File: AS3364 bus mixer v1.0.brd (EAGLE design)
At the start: 44.5 x 32.4 mm, 65 parts, among them IC1 TL072JT, IC2 TL072JT, IC3 TL072JT, IC30 TL072JT, IC4 TL072JT, IC5 79L09F, IC6 78L09F, IC7 CH446Q

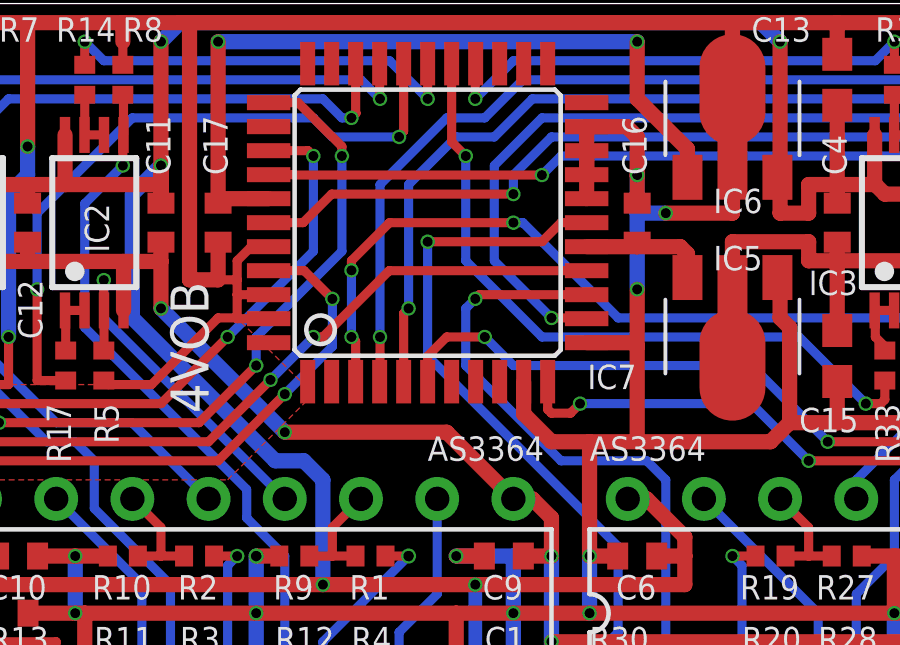
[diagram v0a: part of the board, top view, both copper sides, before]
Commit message: Fixed CH446Q footprint bug for v1.0 of bus mixer
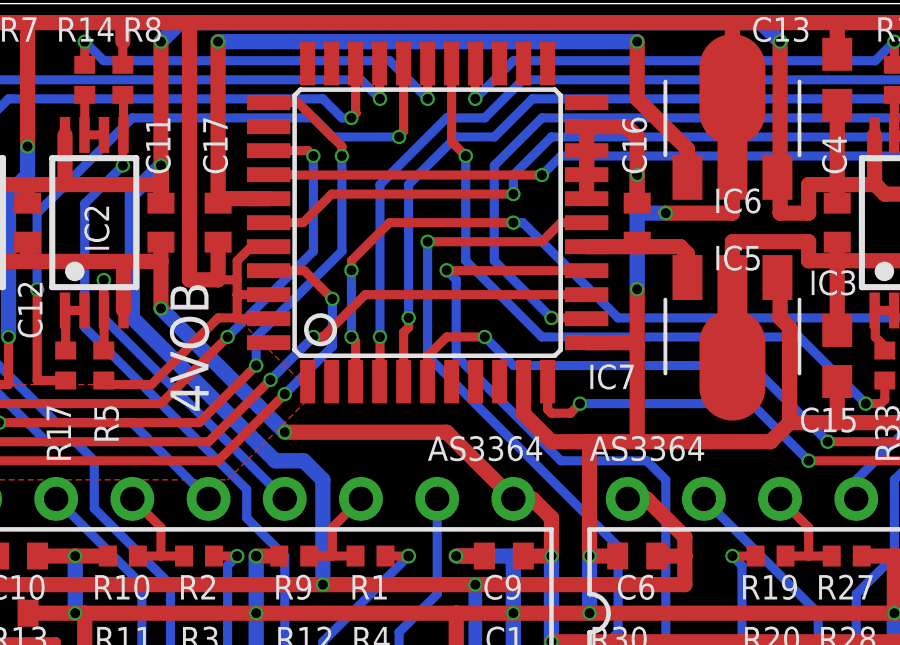
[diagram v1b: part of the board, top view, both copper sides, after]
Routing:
- net BITCRUSH_IN: track 25.4 -> 27.4 mm
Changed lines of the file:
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@@
 <wire x1="42.8625" y1="30.6625" x2="42.8625" y2="32.0675" width="0.3048" layer="1"/>
 <contactref element="SV1" pad="17"/>
+<wire x1="38.1" y1="20.1375" x2="39.6875" y2="21.1375" width="0" layer="19" extent="1-1"/>
 </signal>
 <signal name="OUT4">
@@
 <contactref element="IC30" pad="7"/>
 <wire x1="41.5925" y1="30.6625" x2="41.5925" y2="31.4325" width="0.3048" layer="1"/>
-<wire x1="16.6625" y1="20.1" x2="16.6625" y2="22.3775" width="0.3048" layer="1"/>
-<wire x1="16.6625" y1="22.3775" x2="16.8275" y2="22.5425" width="0.3048" layer="1"/>
-<via x="16.8275" y="22.5425" extent="1-16" drill="0.3302"/>
+<wire x1="16.6625" y1="20.1" x2="16.6625" y2="21.7425" width="0.3048" layer="1"/>
+<wire x1="16.8275" y1="21.9075" x2="16.6625" y2="21.7425" width="0.3048" layer="1"/>
+<wire x1="16.8275" y1="21.9075" x2="16.8275" y2="22.225" width="0.3048" layer="1"/>
+<via x="16.8275" y="22.225" extent="1-16" drill="0.3302"/>
 <via x="41.5925" y="31.4325" extent="1-16" drill="0.3302"/>
 <wire x1="16.8275" y1="26.67" x2="18.415" y2="28.2575" width="0.3048" layer="16"/>
 <wire x1="18.415" y1="28.2575" x2="19.685" y2="28.2575" width="0.3048" layer="16"/>
 <wire x1="19.685" y1="28.2575" x2="20.955" y2="29.5275" width="0.3048" layer="16"/>
-<wire x1="16.8275" y1="22.5425" x2="16.8275" y2="26.67" width="0.3048" layer="16"/>
+<wire x1="16.8275" y1="22.225" x2="16.8275" y2="26.67" width="0.3048" layer="16"/>
 <wire x1="41.9025" y1="28.325" x2="41.91" y2="28.3175" width="0.3048" layer="1"/>
 <wire x1="41.91" y1="28.3175" x2="41.91" y2="27.305" width="0.3048" layer="1"/>
@@
 <wire x1="25.4" y1="7.9375" x2="25.4" y2="16.8275" width="0.3048" layer="16"/>
 <wire x1="25.4" y1="16.8275" x2="24.765" y2="17.4625" width="0.3048" layer="16"/>
-<wire x1="21.9075" y1="17.4625" x2="18.7325" y2="20.6375" width="0.3048" layer="16"/>
-<wire x1="18.7325" y1="20.6375" x2="18.7325" y2="22.5425" width="0.3048" layer="16"/>
-<wire x1="18.7325" y1="22.5425" x2="19.05" y2="22.86" width="0.3048" layer="16"/>
-<via x="19.05" y="22.86" extent="1-16" drill="0.3302"/>
-<wire x1="19.05" y1="22.86" x2="19.19" y2="23" width="0.3048" layer="1"/>
-<wire x1="19.19" y1="23" x2="22.7625" y2="23" width="0.3048" layer="1"/>
+<wire x1="21.9075" y1="17.4625" x2="18.415" y2="20.955" width="0.3048" layer="16"/>
+<via x="18.0975" y="23.8125" extent="1-16" drill="0.3302"/>
 <wire x1="26.035" y1="6.0325" x2="26.035" y2="7.3025" width="0.3048" layer="16"/>
 <wire x1="24.765" y1="17.4625" x2="21.9075" y2="17.4625" width="0.3048" layer="16"/>
 <contactref element="SV1" pad="13"/>
+<wire x1="18.415" y1="20.955" x2="18.415" y2="23.495" width="0.3048" layer="16"/>
+<wire x1="18.415" y1="23.495" x2="18.0975" y2="23.8125" width="0.3048" layer="16"/>
+<wire x1="22.7625" y1="23.8" x2="18.11" y2="23.8" width="0.3048" layer="1"/>
+<wire x1="18.11" y1="23.8" x2="18.0975" y2="23.8125" width="0.3048" layer="1"/>
 </signal>
 <signal name="RST">
@@
 <wire x1="13.6525" y1="21.59" x2="12.22375" y2="20.16125" width="0.3048" layer="16"/>
 <via x="13.6525" y="21.59" extent="1-16" drill="0.3302"/>
-<wire x1="16.18" y1="23.8" x2="13.97" y2="21.59" width="0.3048" layer="1"/>
-<wire x1="13.97" y1="21.59" x2="13.6525" y2="21.59" width="0.3048" layer="1"/>
-<wire x1="16.18" y1="23.8" x2="22.7625" y2="23.8" width="0.3048" layer="1"/>
+<wire x1="13.6525" y1="21.59" x2="13.97" y2="21.59" width="0.3048" layer="1"/>
 <contactref element="SV1" pad="30"/>
+<wire x1="15.38" y1="23" x2="22.7625" y2="23" width="0.3048" layer="1"/>
+<wire x1="13.97" y1="21.59" x2="15.38" y2="23" width="0.3048" layer="1"/>
 </signal>
 </signals>
